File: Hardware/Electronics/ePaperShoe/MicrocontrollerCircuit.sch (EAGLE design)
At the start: 23 parts, among them U2 NRF52832, X1 32MHz, X2 32.768kHz

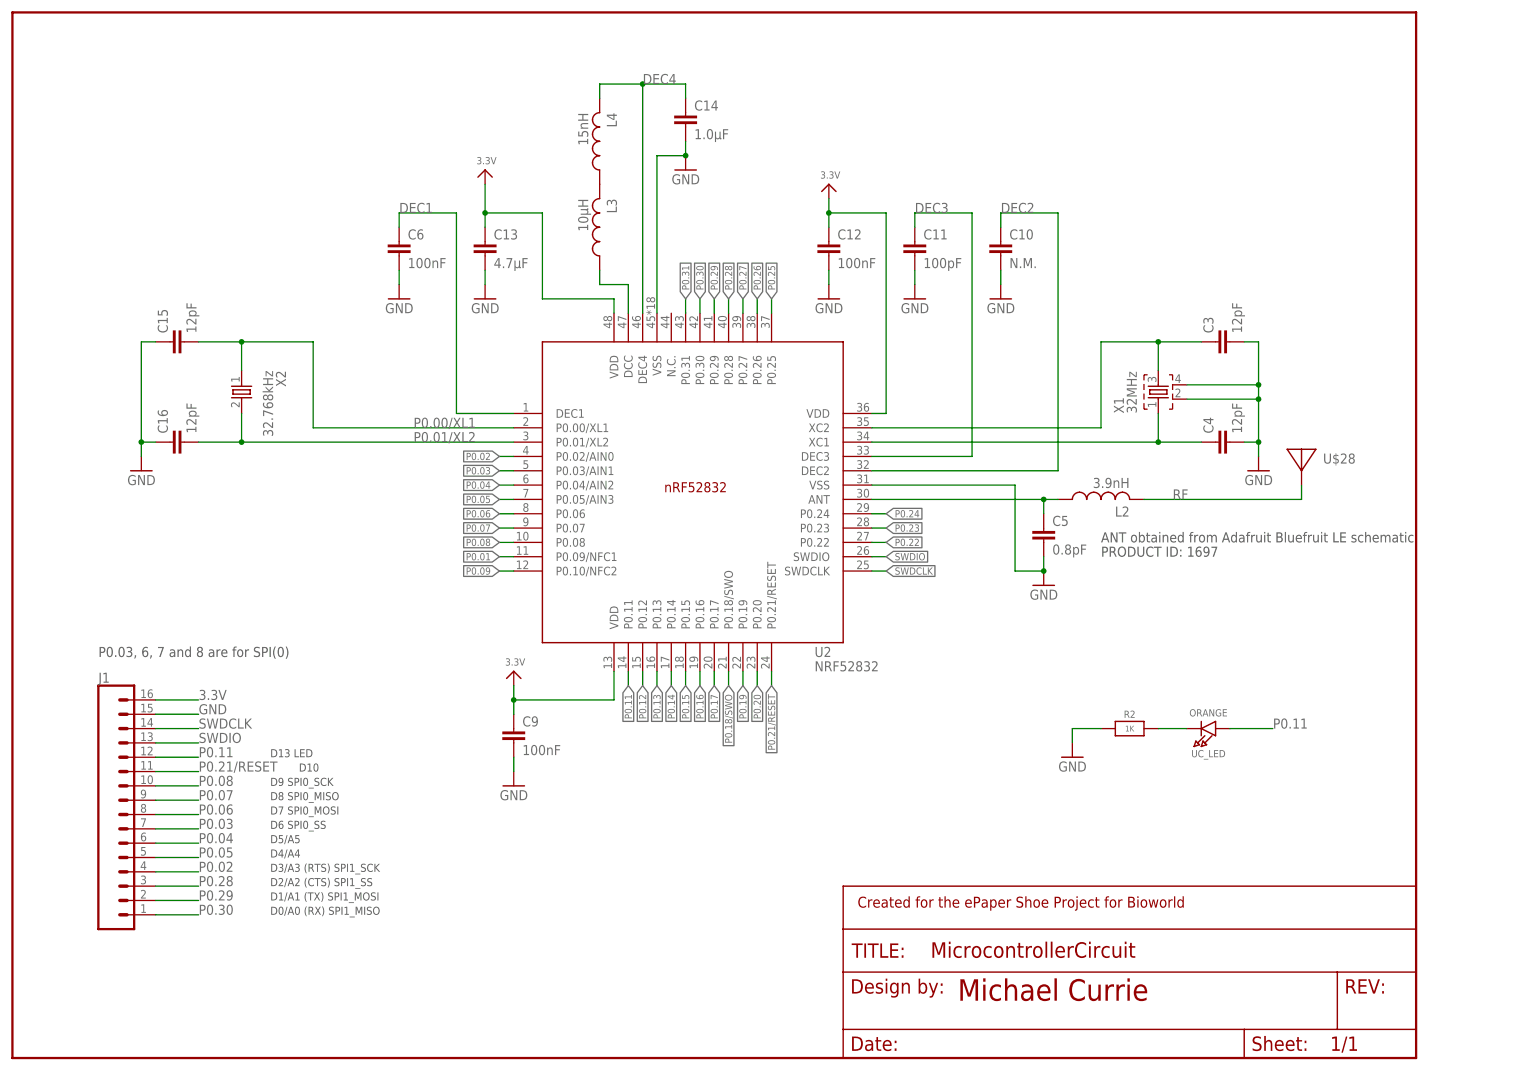
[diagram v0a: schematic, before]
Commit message: Finished design on the nRF52 schematic
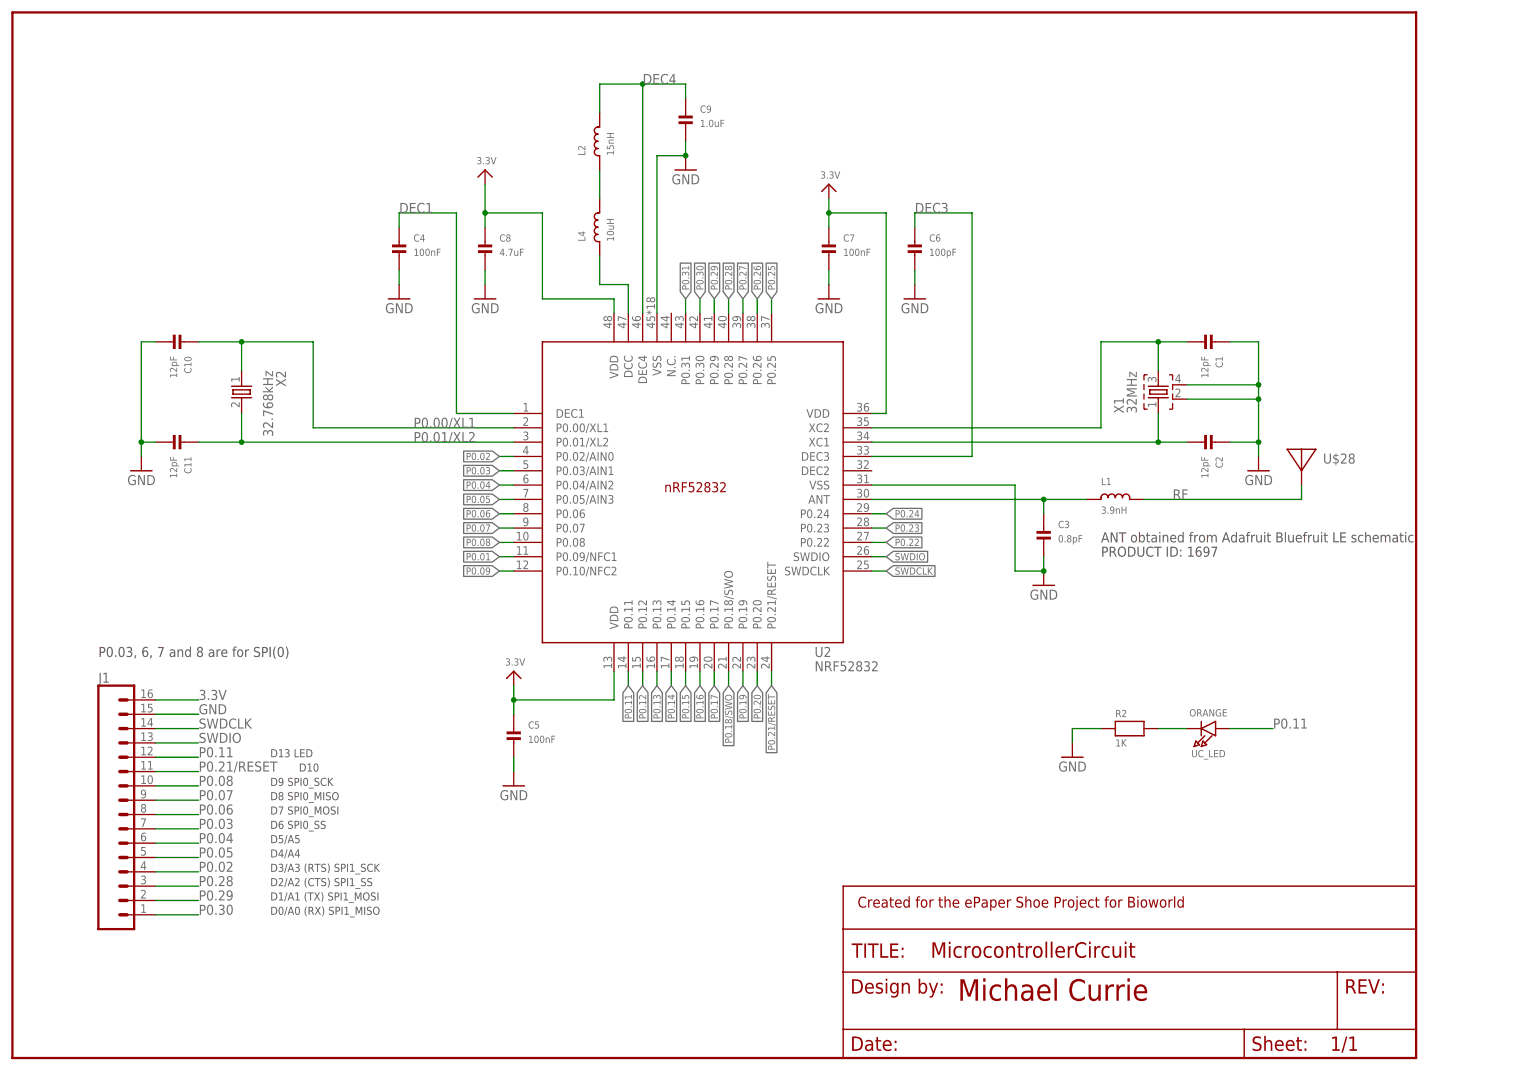
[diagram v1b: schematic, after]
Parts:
- removed C12: 100nF, Nordic_nRF:CAPACITOR_0402_N
- removed C13: 4.7µF, Nordic_nRF:CAPACITOR_0603_N
- removed C14: 1.0µF, Nordic_nRF:CAPACITOR_0603_N
- removed C15, C16: 12pF, Nordic_nRF:CAPACITOR_0402_N
- removed L3: 10µH, Nordic_nRF:INDUCTOR_0603_N
- added C1, C2: 12pF, microbuilder:CAP_CERAMIC1206
- added C7: 100nF, microbuilder:CAP_CERAMIC1206
- added C8: 4.7uF, microbuilder:CAP_CERAMIC1206
- added L1: 3.9nH, microbuilder:INDUCTOR0805
- C10: value N.M. -> 12pF; device Nordic_nRF:CAPACITOR_0402_N -> microbuilder:CAP_CERAMIC1206
- C11: value 100pF -> 12pF; device Nordic_nRF:CAPACITOR_0402_N -> microbuilder:CAP_CERAMIC1206
- C3: value 12pF -> 0.8pF; device Nordic_nRF:CAPACITOR_0402_N -> microbuilder:CAP_CERAMIC1206
- C4: value 12pF -> 100nF; device Nordic_nRF:CAPACITOR_0402_N -> microbuilder:CAP_CERAMIC1206
- C5: value 0.8pF -> 100nF; device Nordic_nRF:CAPACITOR_0402_N -> microbuilder:CAP_CERAMIC1206
- C6: value 100nF -> 100pF; device Nordic_nRF:CAPACITOR_0402_N -> microbuilder:CAP_CERAMIC1206
- C9: value 100nF -> 1.0uF; device Nordic_nRF:CAPACITOR_0402_N -> microbuilder:CAP_CERAMIC1206
- L2: value 3.9nH -> 15nH; device Nordic_nRF:INDUCTOR_0402_N -> microbuilder:INDUCTOR0805
- L4: value 15nH -> 10uH; device Nordic_nRF:INDUCTOR_0402_N -> microbuilder:INDUCTOR0805
- R2: device microbuilder:RESISTOR0805_NOOUTLINE -> microbuilder:RESISTOR0805
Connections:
- removed net DEC2: C10.1, U2.DEC2@32
- removed net N$4: L3.2, L4.1
- new net N$1: L2.1, L4.2
- net 3.3V: now also C5.P$1, C7.P$1, C8.P$1; no longer C12.1, C13.1, C9.1
- net ANT: now also C3.P$1, L1.1; no longer C5.1, L2.1
- net DEC1: now also C4.P$1; no longer C6.1
- net DEC3: now also C6.P$1; no longer C11.1
- net DEC4: now also C9.P$1, L2.2; no longer C14.1, L4.2
- net GND: now also C1.P$1, C10.P$2, C11.P$2, C2.P$1, C3.P$2, C4.P$2, C5.P$2, C6.P$2, C7.P$2, C8.P$2, C9.P$2; no longer C10.2, C11.2, C12.2, C13.2, C14.2, C15.1, C16.1, C3.2, C4.2, C5.2, C6.2, C9.2
- net N$3: now also C1.P$2; no longer C3.1
- net N$5: now also L4.1; no longer L3.1
- net P0.00/XL1: now also C10.P$1; no longer C15.2
- net P0.01/XL2: now also C11.P$1; no longer C16.2
- net RF: now also L1.2; no longer L2.2
- net X1: now also C2.P$2; no longer C4.1
